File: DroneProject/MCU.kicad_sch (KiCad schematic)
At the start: 37 parts, among them U41 STM32F410RBT6, Y41 LFXTAL003151

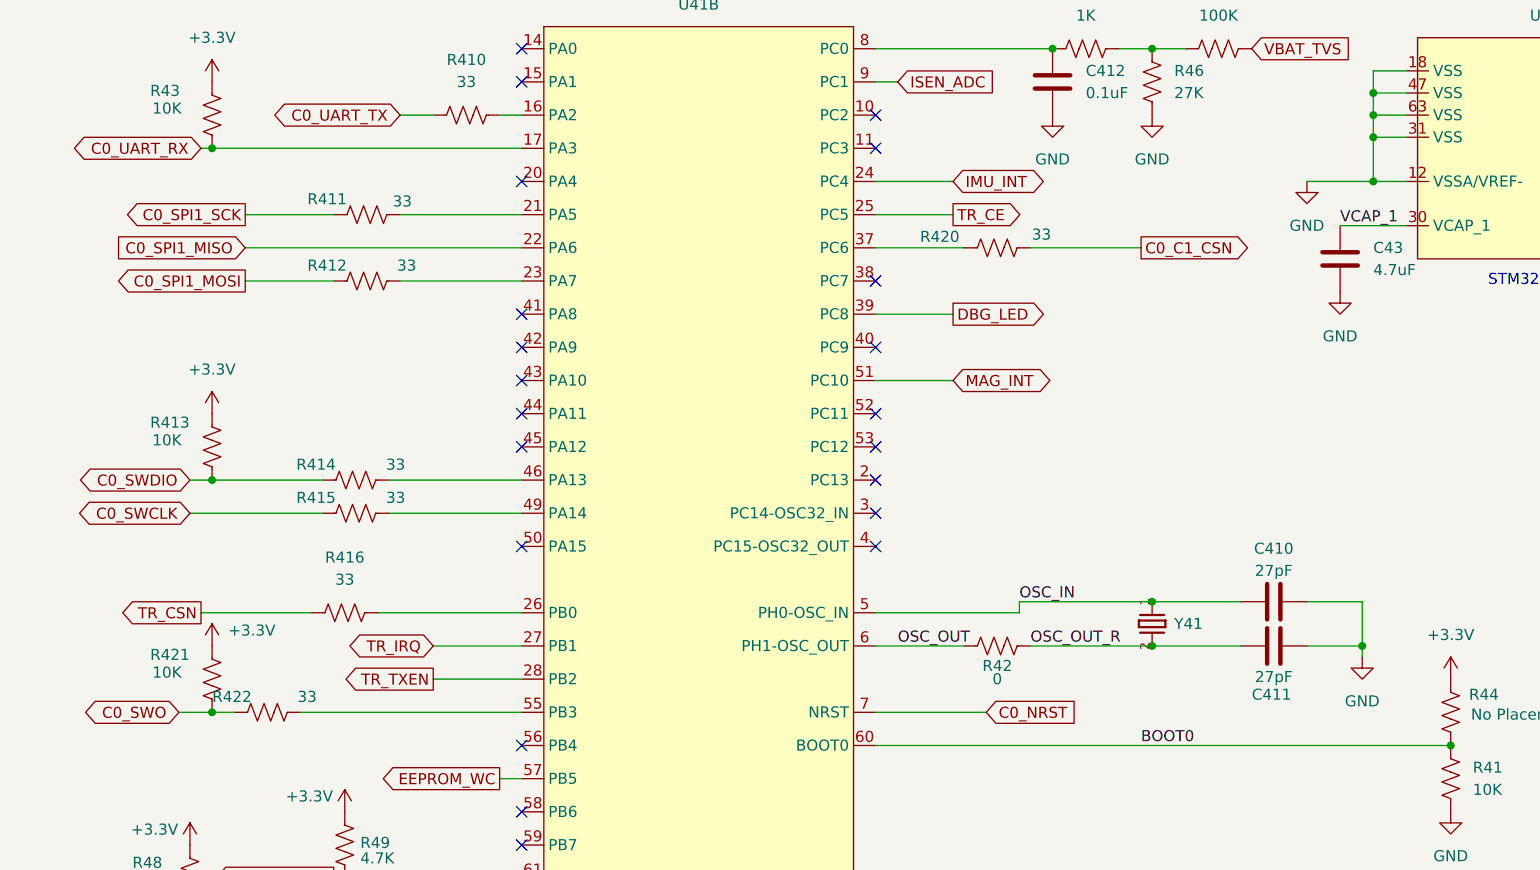
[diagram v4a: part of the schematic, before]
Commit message: Finished most of routing for motor controls, however likely going to revert back and make separate ESC boards for motor control as I think that would honestly be more efficient from both a cost and debug complexity standpoint.
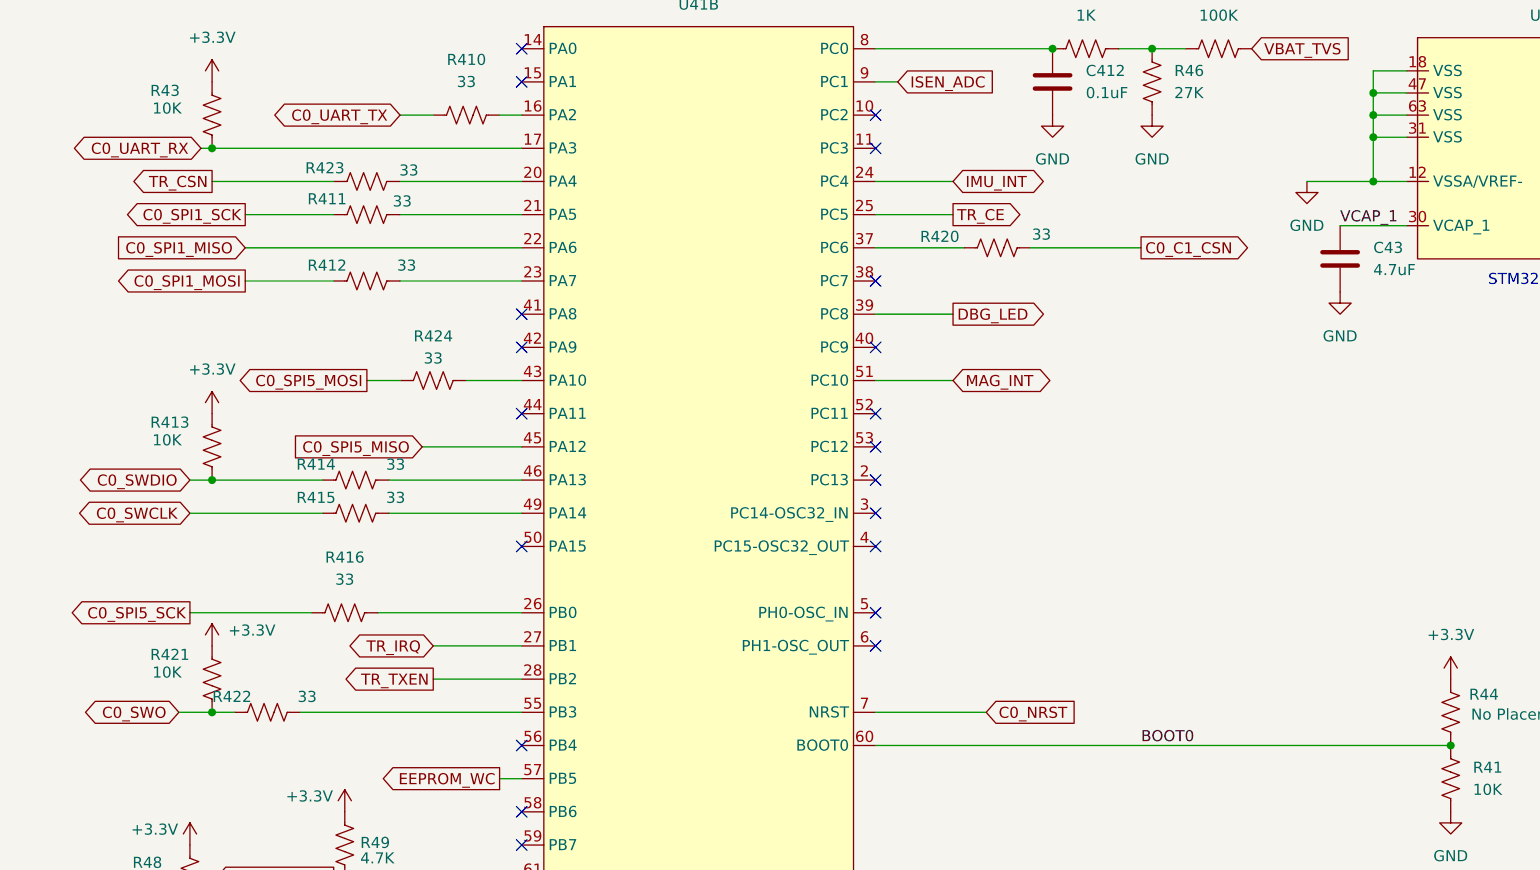
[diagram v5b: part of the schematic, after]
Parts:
- removed C410, C411: 27pF, Capacitor_SMD:C_0603_1608Metric, symbol Device:C
- removed R42: 0, Resistor_SMD:R_0402_1005Metric, symbol Device:R_US
- removed Y41: LFXTAL003151, Library:WE-XTAL_HC49_4HSMX, symbol Global:LFXTAL003151
- added R423, R424: 33, Resistor_SMD:R_0402_1005Metric, symbol Device:R_US
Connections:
- net TR_CSN: now also R423.1; no longer R416.1
- net at U41.20 (PA4): now also R423.2
- net at U41.43 (PA10): now also R424.2
- net C0_SPI5_MISO: now reaches U41.45 (PA12)
- net OSC_IN: no longer names the net of U41.5 (PH0-OSC_IN)
- net OSC_OUT: no longer names the net of U41.6 (PH1-OSC_OUT)
- new net C0_SPI5_MOSI: R424.1
- new net C0_SPI5_SCK: R416.1
- no-connect marks 22 -> 21

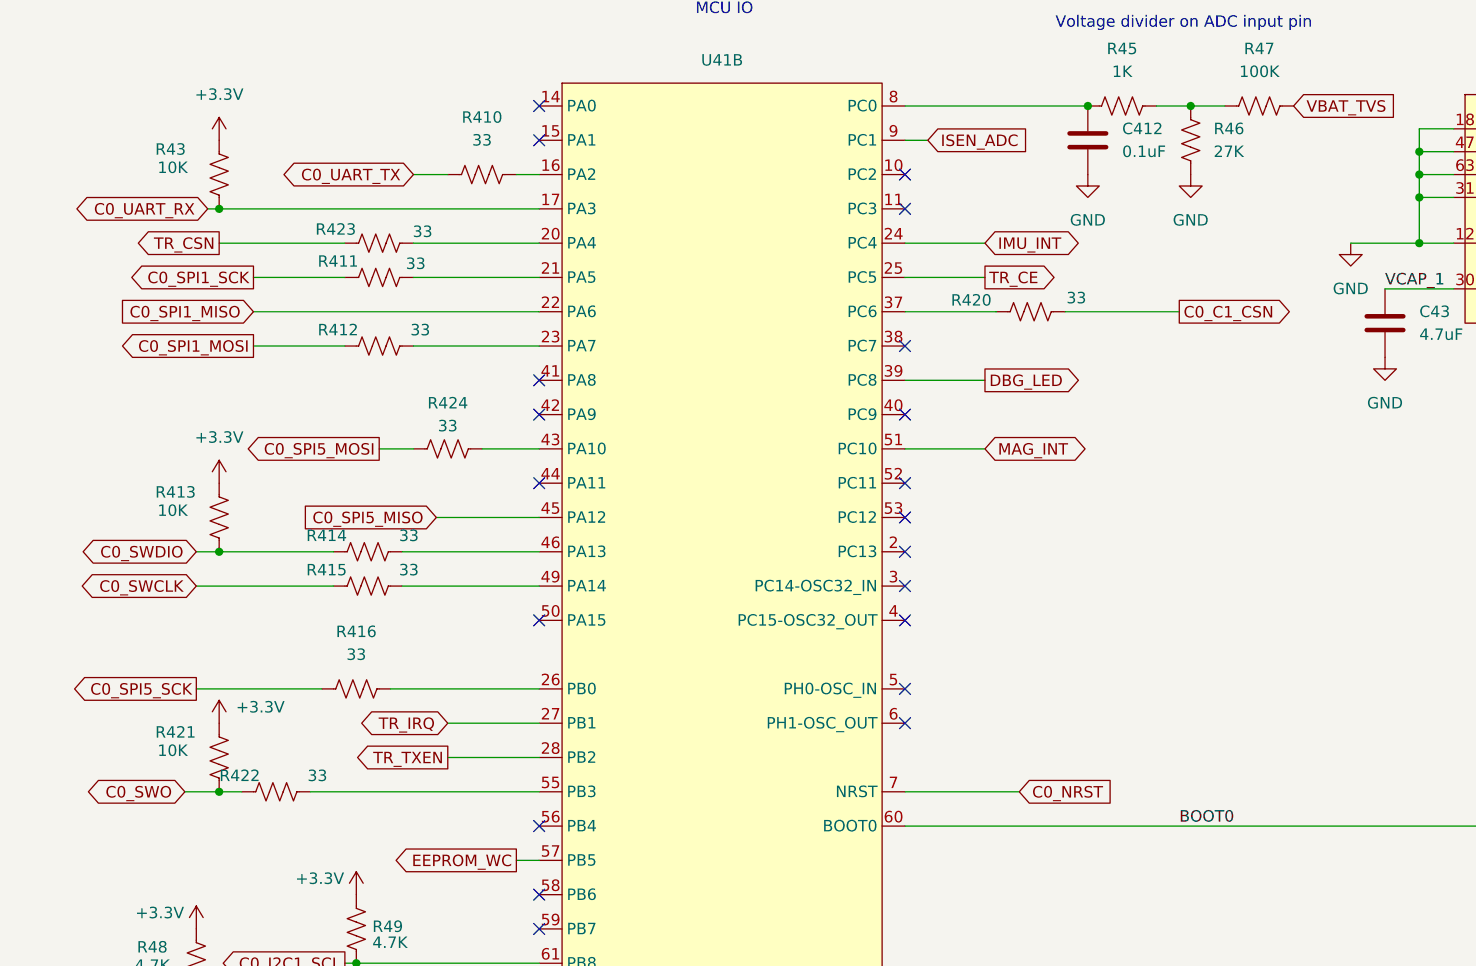
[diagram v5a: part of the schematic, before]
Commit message: Removed C1 and motor controllers from main platform and moved to own project
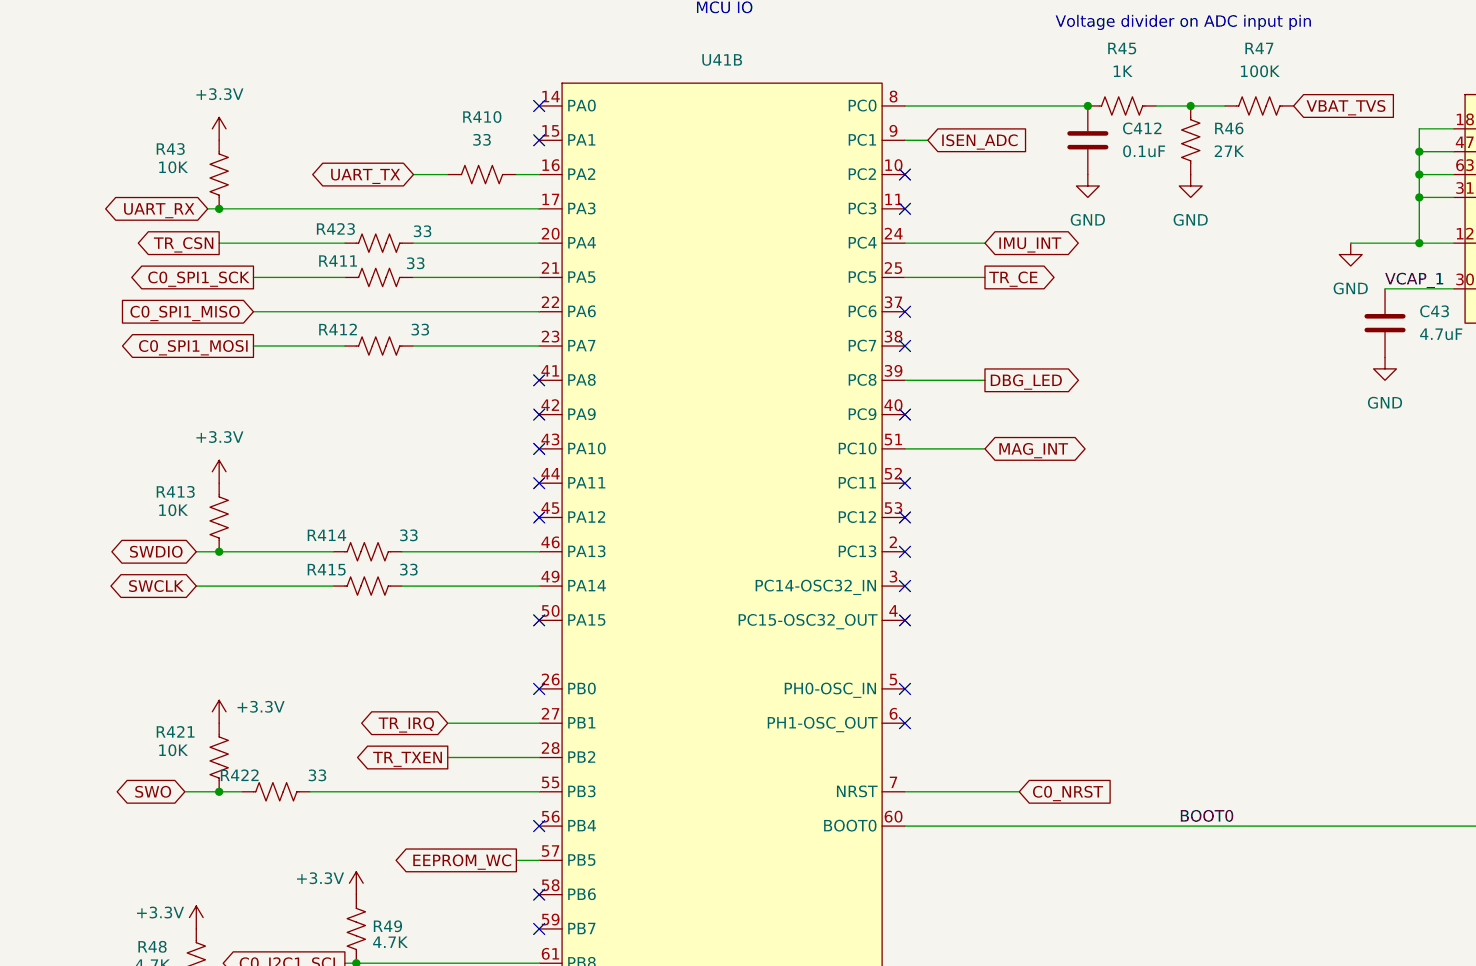
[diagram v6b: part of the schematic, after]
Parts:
- removed R416, R420, R424: 33, Resistor_SMD:R_0402_1005Metric, symbol Device:R_US
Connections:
- net C0_SPI5_MISO: no longer names the net of U41.45 (PA12)
- net C0_SWCLK renamed SWCLK
- net C0_SWDIO renamed SWDIO
- net C0_SWO renamed SWO
- net C0_UART_RX renamed UART_RX
- net C0_UART_TX renamed UART_TX
- no-connect marks 21 -> 25

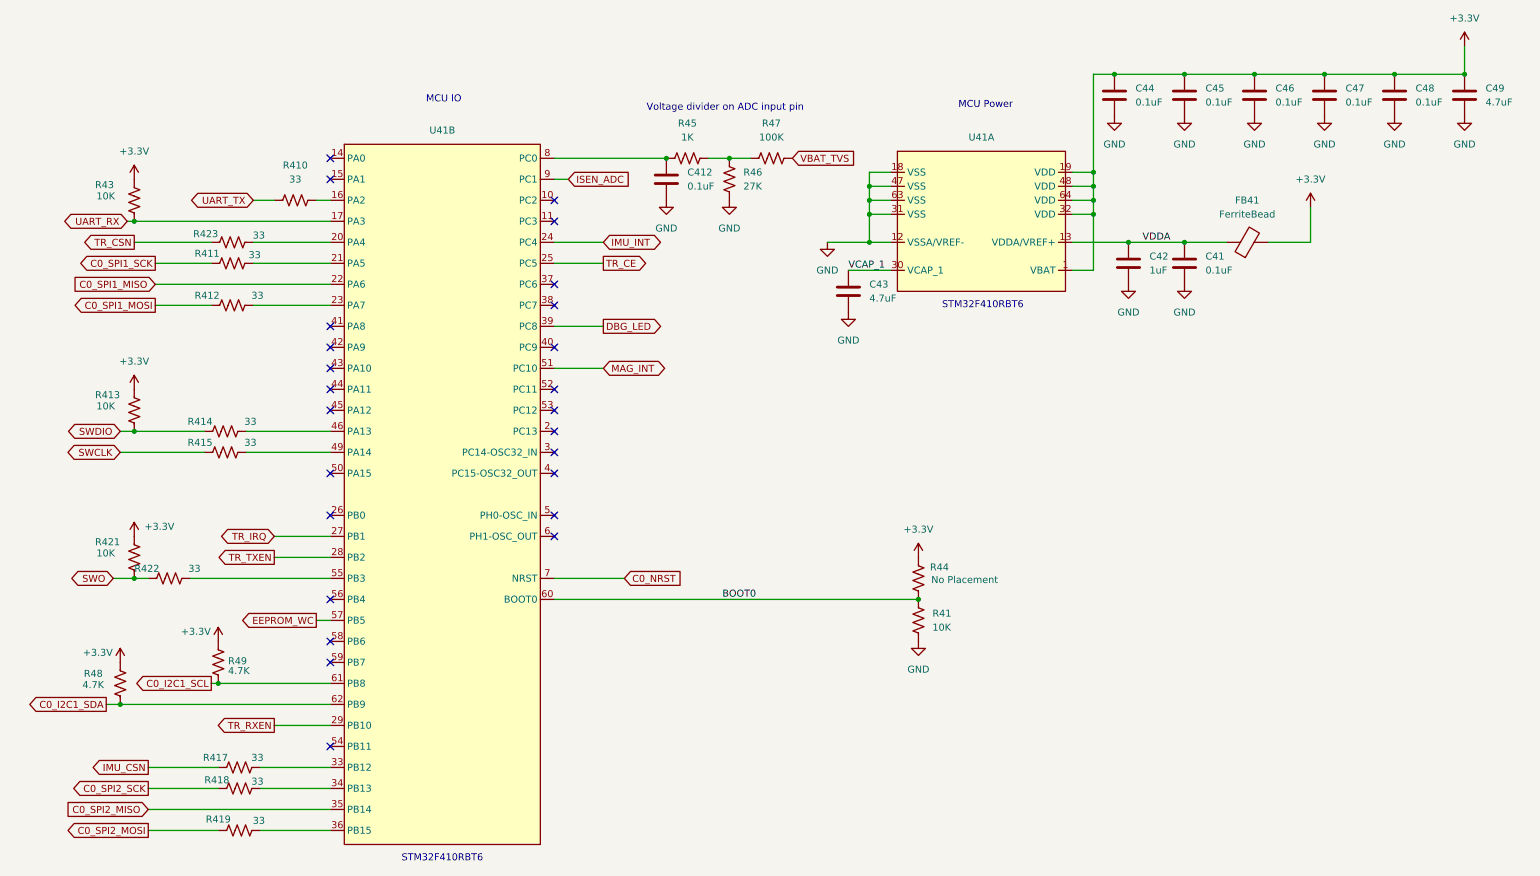
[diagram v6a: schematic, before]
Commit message: Completed schematic for brushless ESC and added needed components to main board.  The plan is to mount the ESCs on the main board using 2.54mm Vert Conn Headers
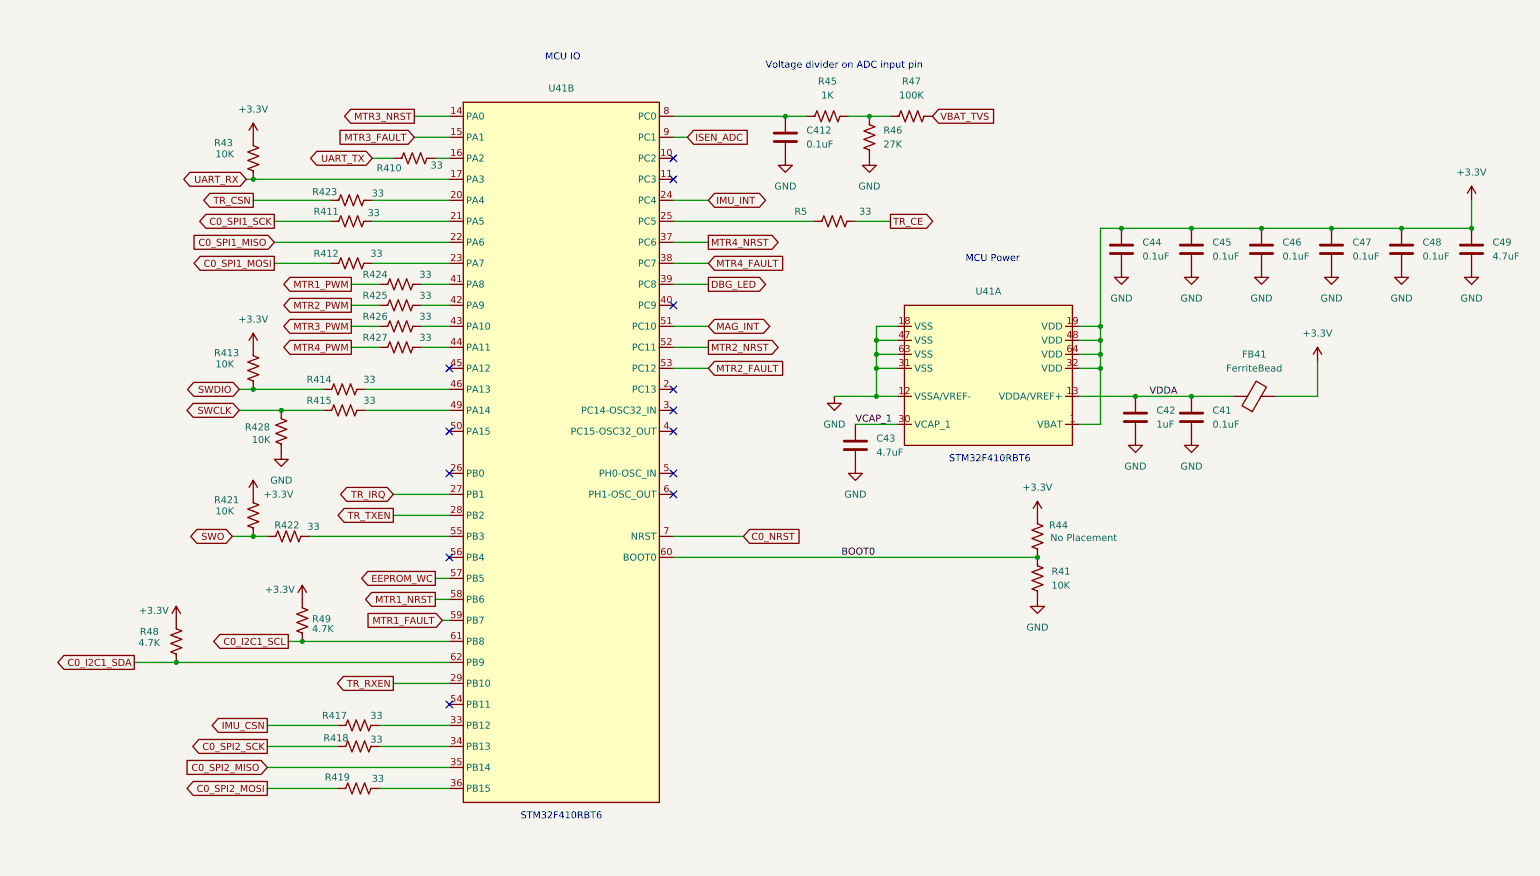
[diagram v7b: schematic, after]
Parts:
- added R424, R425, R426, R427, R5: 33, Resistor_SMD:R_0402_1005Metric, symbol Device:R_US
- added R428: 10K, Resistor_SMD:R_0402_1005Metric, symbol Device:R_US
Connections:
- net GND: now also R428.1
- net SWCLK: now also R428.2
- net TR_CE: now also R5.2; no longer U41.25 (PC5)
- net MTR3_NRST: now reaches U41.14 (PA0)
- net MTR3_FAULT: now reaches U41.15 (PA1)
- net MTR4_NRST: now reaches U41.37 (PC6)
- net MTR4_FAULT: now reaches U41.38 (PC7)
- net at U41.41 (PA8): now also R424.2
- net at U41.42 (PA9): now also R425.2
- net at U41.43 (PA10): now also R426.2
- net at U41.44 (PA11): now also R427.2
- net MTR2_NRST: now reaches U41.52 (PC11)
- net MTR2_FAULT: now reaches U41.53 (PC12)
- net MTR1_NRST: now reaches U41.58 (PB6)
- net MTR1_FAULT: now reaches U41.59 (PB7)
- new net: R5.1, U41.25 (PC5)
- new net MTR1_PWM: R424.1
- new net MTR2_PWM: R425.1
- new net MTR3_PWM: R426.1
- new net MTR4_PWM: R427.1
- no-connect marks 25 -> 13
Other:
- moved on the sheet: C41, C412, C42, C43, C44, C45, C46, C47, C48, C49, FB41, R41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

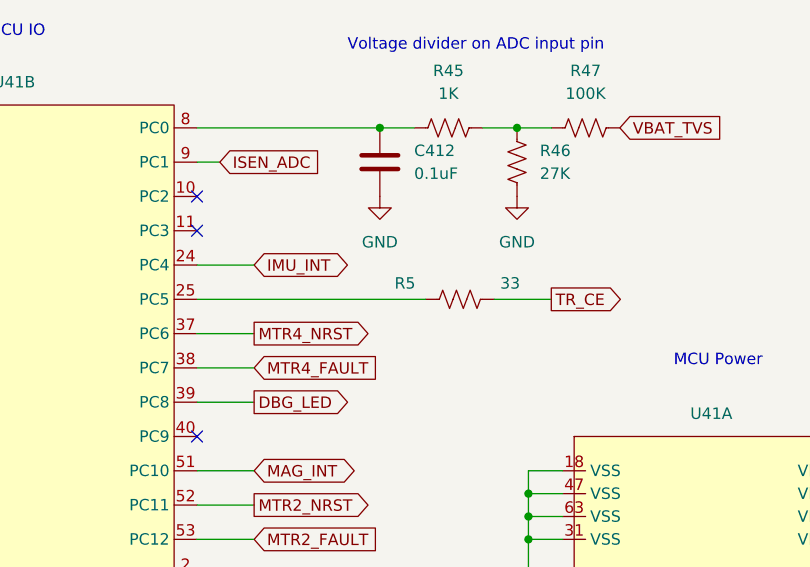
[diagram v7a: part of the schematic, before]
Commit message: Finished layout for controller board
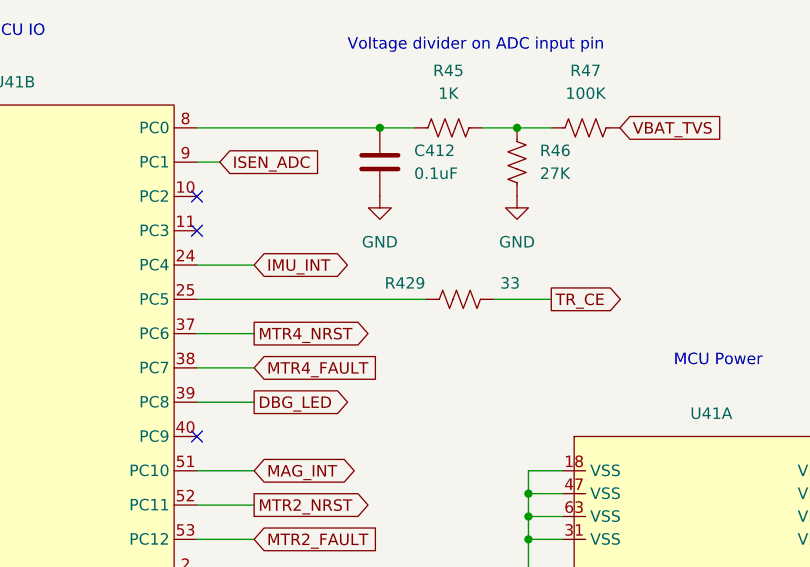
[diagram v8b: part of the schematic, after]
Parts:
- renumbered R5 to R429
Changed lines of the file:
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@@
 		(on_board yes)
 		(dnp no)
-		(property "Reference" "R5"
+		(property "Reference" "R429"
 			(at 153.924 50.292 90)
 			(effects
@@
 			(project "DroneProject"
 				(path "/feb4ca7b-5376-4689-a73b-f56020a5aa30/e25377bf-9845-4f44-9d9e-87e2530b67ae"
-					(reference "R5")
+					(reference "R429")
 					(unit 1)
 				)
